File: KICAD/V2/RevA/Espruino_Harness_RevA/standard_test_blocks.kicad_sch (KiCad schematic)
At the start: 91 parts, among them J201 EXTERNAL_ANALOG_STIMULUS_0_TO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, J301 GROVE_I2C, J302 MCP23017_GPIO, J401 MCP3008_ANALOGUE_BREAKOUT, J402 PIHUT_MICROSD_BREAKOUT_106696, J501 DS18B20_SENSOR_A, J502 DS18B20_SENSOR_B, J503 2K2_DQ_4K7, J504 DS2413_MODULE, J701 UART_PEER_DIAGNOSTIC, J902 PIXEL_SHIFTER_6066, Q301 2N7002, Q302 2N7002, U301 MCP23017-E/SO, U401 MCP3008, U701 TMUX1511

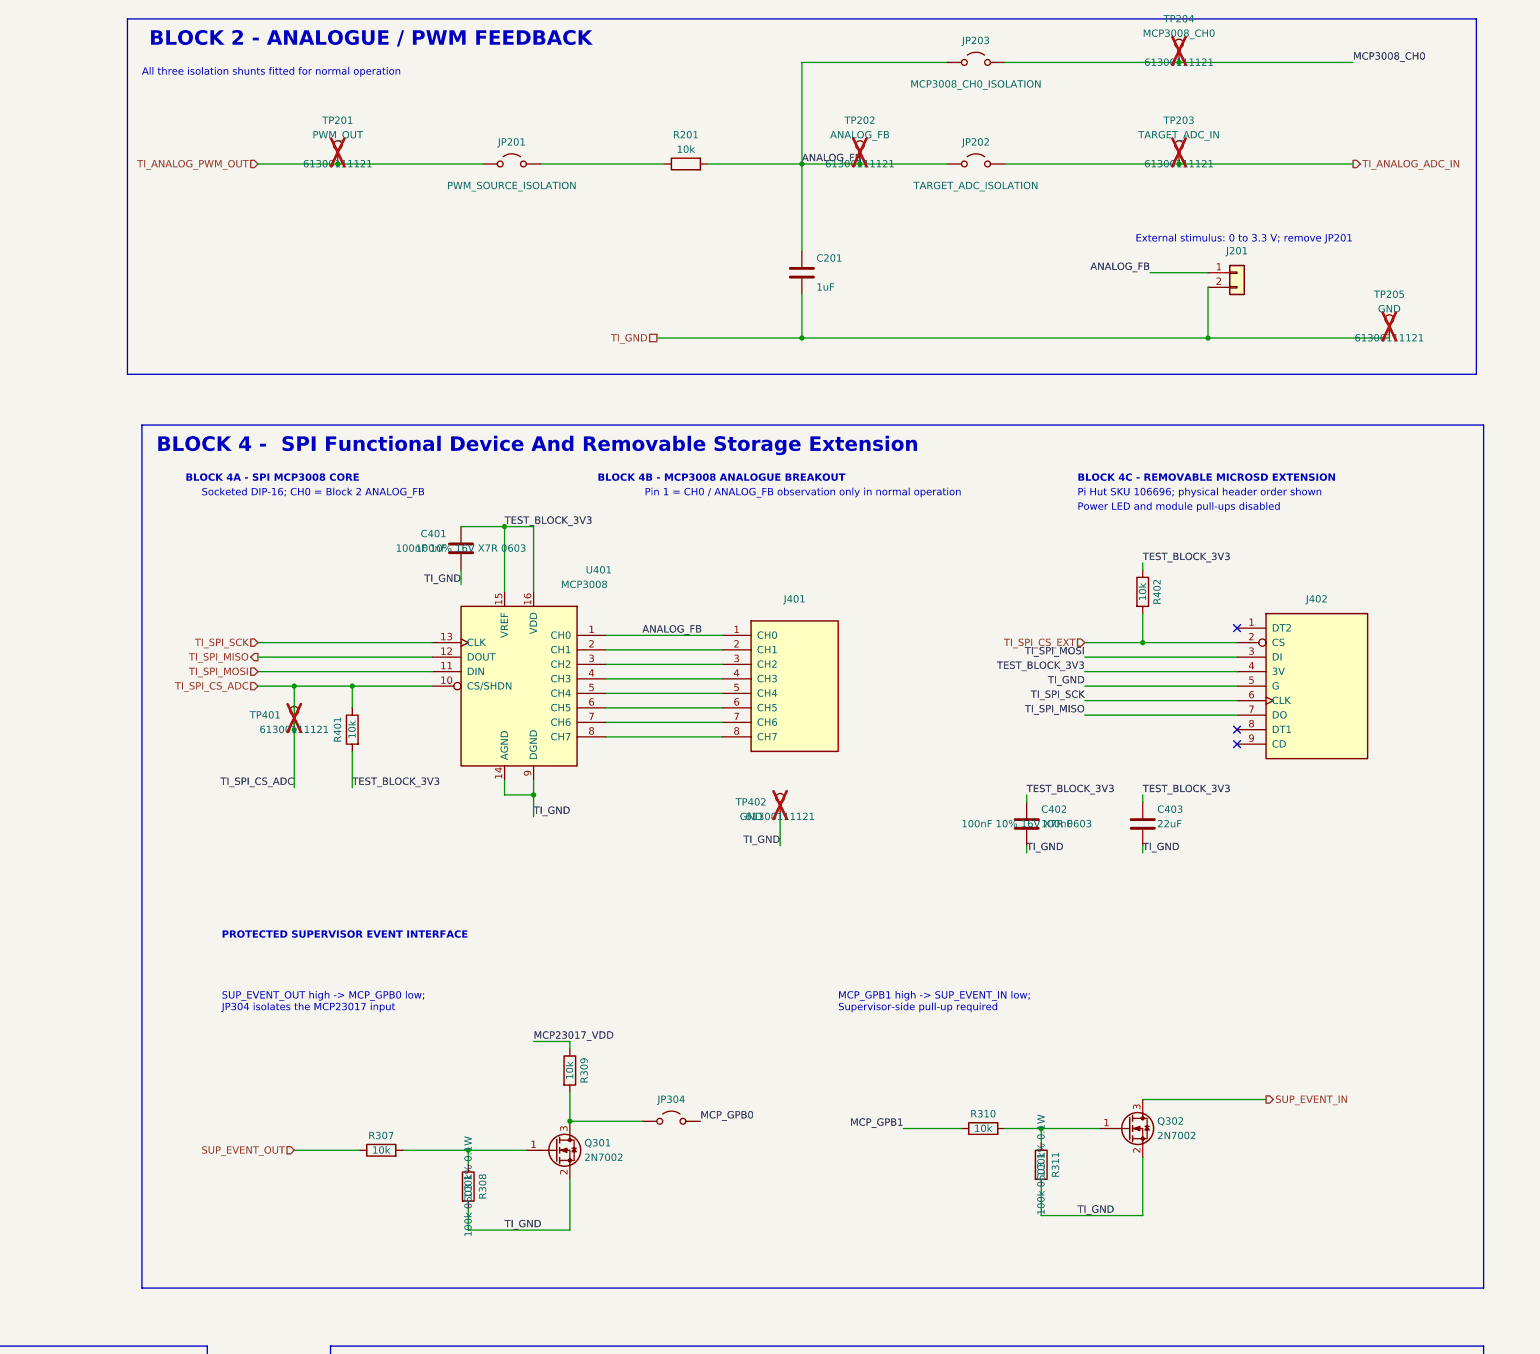
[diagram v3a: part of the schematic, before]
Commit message: Verify TB02 analogue PWM feedback baseline
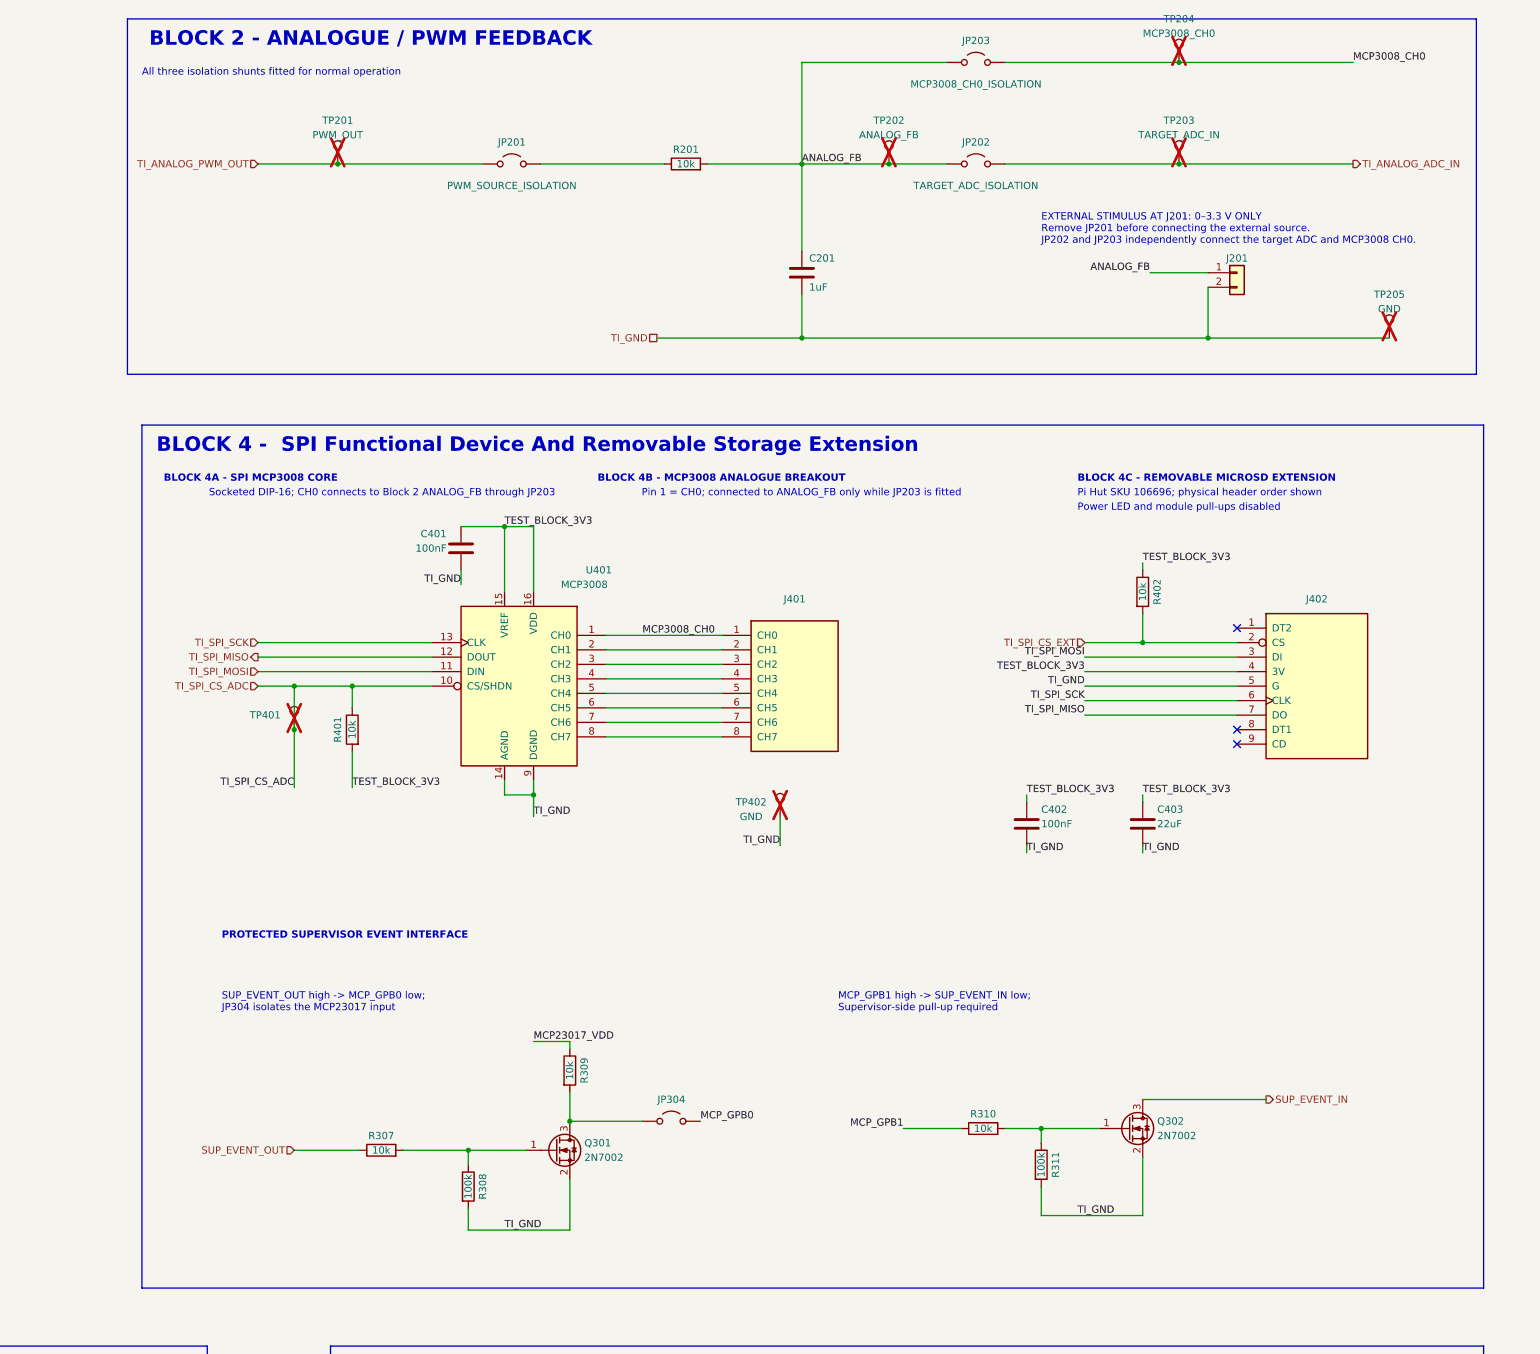
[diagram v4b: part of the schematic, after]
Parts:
- removed JP201: PWM_SOURCE_ISOLATION, Connector_PinHeader_2.54mm:PinHeader_1x02_P2.54mm_Vertical, symbol Jumper:Jumper_2_Open
- removed JP202: TARGET_ADC_ISOLATION, Connector_PinHeader_2.54mm:PinHeader_1x02_P2.54mm_Vertical, symbol Jumper:Jumper_2_Open
- removed JP203: MCP3008_CH0_ISOLATION, Connector_PinHeader_2.54mm:PinHeader_1x02_P2.54mm_Vertical, symbol Jumper:Jumper_2_Open
- added JP201: PWM_SOURCE_ISOLATION, Connector_PinHeader_2.54mm:PinHeader_1x02_P2.54mm_Vertical, symbol Espruino_Harness_RevA:LOOPBACK_ISOLATION_HEADER
- added JP202: TARGET_ADC_ISOLATION, Connector_PinHeader_2.54mm:PinHeader_1x02_P2.54mm_Vertical, symbol Espruino_Harness_RevA:LOOPBACK_ISOLATION_HEADER
- added JP203: MCP3008_CH0_ISOLATION, Connector_PinHeader_2.54mm:PinHeader_1x02_P2.54mm_Vertical, symbol Espruino_Harness_RevA:LOOPBACK_ISOLATION_HEADER
- C201: MPN (none) -> C1608X7R1C105K080AC
- J201: MPN (none) -> 61300211121
- R201: MPN (none) -> RC0603FR-0710KL
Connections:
- net ANALOG_FB: now also JP202.1 (A), JP203.1 (A); no longer J401.1 (CH0), U401.1 (CH0)
- net MCP3008_CH0: now also J401.1 (CH0), U401.1 (CH0), JP203.2 (B)
- net TI_ANALOG_ADC_IN: now also JP202.2 (B)
- net TI_ANALOG_PWM_OUT: now also JP201.1 (A)
- net at R201.1: now also JP201.2 (B)
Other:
- note added: "EXTERNAL STIMULUS AT J201: 0–3.3 V ONLY Remove JP201 before connecting the external source. JP202 and JP203 independently connect the target ADC and MCP3008 CH0."
- note added: "Pin 1 = CH0; connected to ANALOG_FB only while JP203 is fitted"
- note added: "Socketed DIP-16; CH0 connects to Block 2 ANALOG_FB through JP203"
- note removed: "External stimulus: 0 to 3.3 V; remove JP201"
- note removed: "Pin 1 = CH0 / ANALOG_FB observation only in normal operation"
- note removed: "Socketed DIP-16; CH0 = Block 2 ANALOG_FB"
- moved on the sheet: TP202

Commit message: Verify TB03 I2C functional device baseline
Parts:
- added R312: 10k, Resistor_SMD:R_0603_1608Metric, symbol Device:R
- J301: footprint (none) -> Espruino_Harness_RevA:Grove_1x04_P2mm_RightAngle_Seeed_320110034; MPN (none) -> 1125R-4P; now not fitted
- J302: MPN (none) -> 61301621121; now not fitted
- JP301, JP302, JP303, JP307, JP308, JP309: symbol Jumper:Jumper_2_Open -> Espruino_Harness_RevA:Jumper_2_Open; MPN (none) -> 61300211121; SHUNT_MPN (none) -> 60900213421
- JP304: MPN (none) -> 61300211121
- JP306: symbol Jumper:Jumper_2_Open -> Espruino_Harness_RevA:Jumper_2_Open; MPN (none) -> 61300211121
- Q301, Q302: AISLER_MPN (none) -> 2N7002LT1G; MPN (none) -> 2N7002LT1G
- R301, R302, R303, R304: AISLER_MPN (none) -> 4.7k 0603 1% 0.1W
- R305: AISLER_MPN (none) -> 470R 0603 1% 0.1W
- R306, R307, R309, R310: AISLER_MPN (none) -> 10k 0603 1% 0.1W
- U301: AISLER_MPN (none) -> MCP23017-E/SO; MPN (none) -> MCP23017-E/SO
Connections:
- net IP03_TEST_BLOCK_SDA: now also J301.2 (SDA), JP302.2 (B), R301.2, R303.2, TP301.1; no longer JP302.1 (A)
- net IP04_TEST_BLOCK_SCL: now also J301.1 (SCL), JP303.2 (B), R302.2, R304.2, TP302.1; no longer JP303.1 (A)
- net MCP23017_RESET_N: now also R306.1; no longer R306.2
- net MCP23017_VDD: now also R306.2, R312.2
- net TEST_BLOCK_3V3: no longer R306.1
- net SCL_PULLUP_SUPPLY: now reaches JP309.1 (A), R302.1, R304.1
- net SDA_PULLUP_SUPPLY: now reaches JP308.1 (A), R301.1, R303.1
- net MCP23017_INTA: now reaches JP307.2 (B), U301.20 (INTA)
- net MCP23017_INTA: now also R312.1
- removed net I2C_SCL_BUS: J301.1 (SCL), JP303.2 (B), R302.2, R304.2, TP302.1, U301.12 (SCL)
- removed net I2C_SDA_BUS: J301.2 (SDA), JP302.2 (B), R301.2, R303.2, TP301.1, U301.13 (SDA)
- new net MCP23017_SCL: JP303.1 (A), U301.12 (SCL)
- new net MCP23017_SDA: JP302.1 (A), U301.13 (SDA)
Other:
- note added: "1"
- note added: "2"
- note added: "FUNCTIONAL FLOW Target-owned I2C ↔ IP03/IP04 ↔ shared SDA/SCL bus Shared bus ↔ Grove J301 Shared bus → JP302/JP303 → U301 U301 GPA0 → R305 → JP306 → TI_I2C_FB U301 GPA1 ↔ GPA2 provides internal interrupt stimulus U301 INTA → JP307 → TI_I2C_INT"
- note added: "INTERRUPT PATH R312 pulls INTA up to MCP23017_VDD. INTA → JP307 → TI_I2C_INT; configure MIRROR=1 and ODR=1. INTB is unconnected; direct probe at U301 pin 19."
- note added: "ISOLATED DEVICE SUPPLY JP301 powers U301, C301, the R306 RESET pull-up and the R312 INTA pull-up from MCP23017_VDD. Opening JP301 removes all local U301 bias."
- note added: "J301: 1=SCL, 2=SDA, 3=3V3, 4=GND. 3.3 V I2C devices only; unplug J301 to isolate the external branch."
- note added: "J302 exposes GPA0–GPA7 and GPB0–GPB7 for observation and experiments. GPA7 and GPB7 are output-only on the selected MCP23017. Do not externally drive pins already assigned to Block 3 functions."
- note added: "JP302/JP303 isolate U301 only. The Grove branch, pull-ups and SDA/SCL test points remain on the shared bus."
- note added: "MCP23017 DEVICE ISOLATION JP301: VDD JP302: SDA JP303: SCL JP304: SUP_EVENT_OUT JP306: FB JP307: INTA All six shunts are fitted for normal operation."
- note added: "MCP_GPB1 high → Q302 on → SUP_EVENT_IN low. The Supervisor side provides the pull-up."
- note added: "NORMAL: JP308/JP309 fitted; R301/R302 provide 4.7k SDA/SCL pull-ups. R303/R304 are DNP parallel adjustment positions. Remove the respective shunt to disable a pull-up group."
- note added: "SUP_EVENT_OUT high → Q301 on → MCP_GPB0 low. JP304 isolates the MCP23017 input."
- note removed: "INTA → TI_I2C_INT; INTA/INTB mirrored open-drain;"
- note removed: "MCP_GPB1 high -> SUP_EVENT_IN low; Supervisor-side pull-up required"
- note removed: "R301/R302: 4.7k fitted; R303/R304: 4.7k DNP"
- note removed: "SUP_EVENT_OUT high -> MCP_GPB0 low; JP304 isolates the MCP23017 input"
- moved on the sheet: R301, R302, R303, R304, R306, TP301, TP302, TP303, TP304, TP305, TP306

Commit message: Verify TB04 SPI and fixed microSD baseline
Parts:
- removed J402: PIHUT_MICROSD_BREAKOUT_106696, Connector_PinHeader_2.54mm:PinHeader_1x09_P2.54mm_Vertical, symbol Espruino_Harness_RevA:PiHut_MicroSD_Breakout_1x09
- added J402: ADAFRUIT_MICROSD_BFF_5683, Espruino_Harness_RevA:Adafruit_MicroSD_BFF_5683_Underside, symbol Espruino_Harness_RevA:Adafruit_MicroSD_BFF_5683
- added TP403: TI_SPI_SCK, Connector_PinHeader_2.54mm:PinHeader_1x01_P2.54mm_Vertical, symbol Connector:TestPoint
- added TP404: TI_SPI_MOSI, Connector_PinHeader_2.54mm:PinHeader_1x01_P2.54mm_Vertical, symbol Connector:TestPoint
- added TP405: TI_SPI_MISO, Connector_PinHeader_2.54mm:PinHeader_1x01_P2.54mm_Vertical, symbol Connector:TestPoint
- added TP406: TI_SPI_CS_EXT, Connector_PinHeader_2.54mm:PinHeader_1x01_P2.54mm_Vertical, symbol Connector:TestPoint
- added TP407: TEST_BLOCK_3V3, Connector_PinHeader_2.54mm:PinHeader_1x01_P2.54mm_Vertical, symbol Connector:TestPoint
- C401: value 100nF -> 1uF; AISLER_MPN 100nF 10% 16V X7R 0603 -> 1uF 10% 16V X7R 0603
- C403: AISLER_MPN (none) -> 22uF 20% 10V X7R 0805
- J401: AISLER_MPN (none) -> 61300811121; MPN (none) -> 61300811121; now not fitted
- R401, R402: AISLER_MPN (none) -> 10k 0603 1% 0.1W
- U401: AISLER_MPN (none) -> MCP3008-I/P; MPN (none) -> MCP3008-I/P; now not fitted
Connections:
- net TEST_BLOCK_3V3: now also J402.4 (3V3), TP407.1
- net TI_GND: now also J402.5 (GND)
- net TI_SPI_CS_EXT: now also J402.6 (CS_TX), TP406.1
- net TI_SPI_MISO: now also J402.2 (MISO), TP405.1
- net TI_SPI_MOSI: now also J402.3 (MOSI), TP404.1
- net TI_SPI_SCK: now also J402.1 (SCK), TP403.1
- no-connect marks 5 -> 2
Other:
- note added: "BLOCK 4 - SPI FUNCTIONAL DEVICE AND FIXED MICROSD STORAGE EXTENSION"
- note added: "BLOCK 4 OBSERVATION POINTS"
- note added: "BLOCK 4C - FIXED UNDERSIDE MICROSD STORAGE EXTENSION J402: Adafruit microSD BFF, Product 5683 / supplier reference ADA5683 3.3 V SPI; factory TX-to-CS jumper closed; RX/A0/A1 alternatives open Required hand-fitted part: DNP for AISLER assembly Orient CARD ACCESS toward the harness-card top edge"
- note added: "For PCB placement, put C402 closest to J402’s 3V3/GND lands, with C403 immediately nearby."
- note added: "J402 footprint deliberately has copper and mask openings but no paste apertures, because all fourteen castellated lands are manually soldered."
- note added: "PROTECTED SUPERVISOR EVENT INTERFACES"
- note added: "R401/R402 keep the MCP3008 and microSD BFF chip selects high/inactive while the target is absent, resetting or unconfigured."
- note removed: "BLOCK 4 - SPI Functional Device And Removable Storage Extension"
- note removed: "BLOCK 4C - REMOVABLE MICROSD EXTENSION"
- note removed: "PROTECTED SUPERVISOR EVENT INTERFACE"
- note removed: "Pi Hut SKU 106696; physical header order shown"
- note removed: "Power LED and module pull-ups disabled"
- moved on the sheet: C401, C402, C403, R309, R402, TP402
